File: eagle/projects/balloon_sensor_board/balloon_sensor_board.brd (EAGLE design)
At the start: 18 x 14 mm, 17 parts, among them J201 MOL-SL-4-RA, U201 PCT2075GVJ, U202 MS560702BA03-50

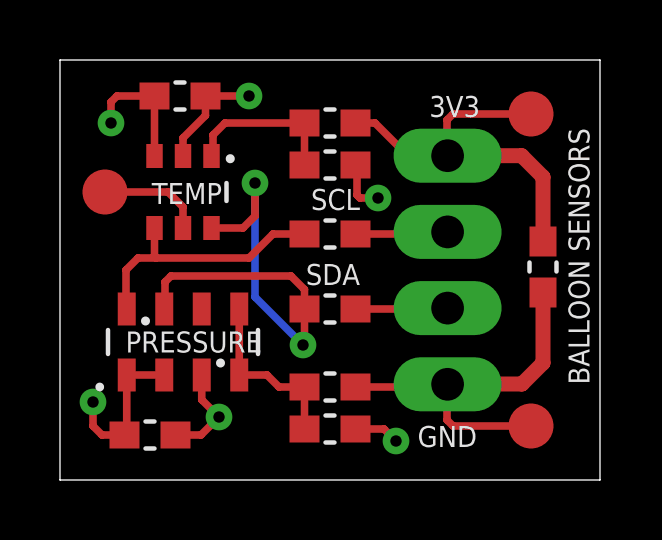
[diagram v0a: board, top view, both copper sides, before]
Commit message: adding all finalized gerber, schem, and bom files for Rev1 of HAT and balloon sensor boards
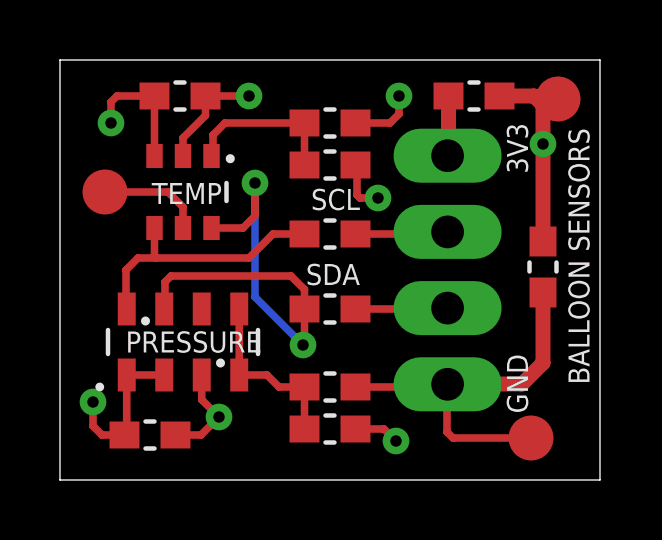
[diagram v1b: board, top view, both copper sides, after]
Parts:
- added R1: 0.0, daqcs:R0603
- moved TP201 1.03 mm to (16.6, 12.7)
- moved TP202 0.40 mm to (15.7, 1.40)
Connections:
- new net PP3V3_R: J201.1, R1.1
- net PP3V3: now also R1.2; no longer J201.1
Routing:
- net PP3V3: track 24.2 -> 20.0 mm, vias 3 -> 5
- net PP3V3_R: track 0.00 -> 2.00 mm

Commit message: added modified BOMs to remove non-component parts, samples, and column for a board instance multiplier
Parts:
- added BOM1: SL 70066 4PIN HOUSING, daqcs:BLANK
- added BOM2, BOM3, BOM4, BOM5: SL 70058 GOLD CRIMP, daqcs:BLANK
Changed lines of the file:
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@@
 </attributes>
 <variantdefs>
-<variantdef name="POR" current="yes"/>
+<variantdef name="POR"/>
 </variantdefs>
 <classes>
@@
 <attribute name="VALUE" x="17.119" y="11.692" size="0.254" layer="27" ratio="6"/>
 </element>
-<element name="R205" library="daqcs" package="R0603" value="0.0" x="9" y="11.9" populate="no" smashed="yes">
+<element name="R205" library="daqcs" package="R0603" value="0.0" x="9" y="11.9" smashed="yes">
 <attribute name="MANUFACTURER" value="Panasonic" x="9" y="11.9" size="1.778" layer="27" display="off"/>
 <attribute name="POWER" value="1/10W" x="9" y="11.9" size="1.778" layer="27" display="off"/>
@@
 <attribute name="VENDOR" value="Digi-key" x="9" y="11.9" size="1.778" layer="27" display="off"/>
 </element>
-<element name="R203" library="daqcs" package="R0603" value="0.0" x="9" y="1.7" populate="no" smashed="yes">
+<element name="R203" library="daqcs" package="R0603" value="0.0" x="9" y="1.7" smashed="yes">
 <attribute name="MANUFACTURER" value="Panasonic" x="9" y="1.7" size="1.778" layer="27" display="off"/>
 <attribute name="POWER" value="1/10W" x="9" y="1.7" size="1.778" layer="27" display="off"/>
@@
 <attribute name="MANUFACTURER_PN" value="ERJ-3GEY0R00V" x="13.8" y="12.8" size="1.778" layer="27" display="off"/>
 </element>
+<element name="BOM1" library="daqcs" package="BLANK" value="SL 70066 4PIN HOUSING" x="18.8" y="13.7">
+<attribute name="MANUFACTURER_PN" value="0050579404" x="18.8" y="13.7" size="1.778" layer="27" display="off"/>
+<attribute name="MANUFACTURER" value="Molex" x="18.8" y="13.7" size="1.778" layer="27" display="off"/>
+<attribute name="DATASHEET" value="HW/docs/projects/raspi_zero_power_sensor_hat/datasheets/connectors/uart_1wire_power_battery/050579402_sd.pdf" x="18.8" y="13.7" size="1.778" layer="27" display="off"/>
+<attribute name="VENDOR_PN" value="WM2902-ND" x="18.8" y="13.7" size="1.778" layer="27" display="off"/>
+<attribute name="VENDOR" value="Digi-key" x="18.8" y="13.7" size="1.778" layer="27" display="off"/>
+</element>
+<element name="BOM2" library="daqcs" package="BLANK" value="SL 70058 GOLD CRIMP" x="18.9" y="12.7">
+<attribute name="MANUFACTURER_PN" value="0016020087" x="18.9" y="12.7" size="1.778" layer="27" display="off"/>
+<attribute name="MANUFACTURER" value="Molex" x="18.9" y="12.7" size="1.778" layer="27" display="off"/>
+<attribute name="DATASHEET" value="HW/docs/projects/raspi_zero_power_sensor_hat/datasheets/connectors/uart_1wire_power_battery/016020087_sd.pdf" x="18.9" y="12.7" size="1.778" layer="27" display="off"/>
+<attribute name="VENDOR_PN" value="WM2512CT-ND" x="18.9" y="12.7" size="1.778" layer="27" display="off"/>
+<attribute name="VENDOR" value="Digi-key" x="18.9" y="12.7" size="1.778" layer="27" display="off"/>
+</element>
+<element name="BOM3" library="daqcs" package="BLANK" value="SL 70058 GOLD CRIMP" x="19" y="12">
+<attribute name="MANUFACTURER_PN" value="0016020087" x="19" y="12" size="1.778" layer="27" display="off"/>
+<attribute name="MANUFACTURER" value="Molex" x="19" y="12" size="1.778" layer="27" display="off"/>
+<attribute name="DATASHEET" value="HW/docs/projects/raspi_zero_power_sensor_hat/datasheets/connectors/uart_1wire_power_battery/016020087_sd.pdf" x="19" y="12" size="1.778" layer="27" display="off"/>
+<attribute name="VENDOR_PN" value="WM2512CT-ND" x="19" y="12" size="1.778" layer="27" display="off"/>
+<attribute name="VENDOR" value="Digi-key" x="19" y="12" size="1.778" layer="27" display="off"/>
+</element>
+<element name="BOM4" library="daqcs" package="BLANK" value="SL 70058 GOLD CRIMP" x="19.1" y="11.3">
+<attribute name="MANUFACTURER_PN" value="0016020087" x="19.1" y="11.3" size="1.778" layer="27" display="off"/>
+<attribute name="MANUFACTURER" value="Molex" x="19.1" y="11.3" size="1.778" layer="27" display="off"/>
+<attribute name="DATASHEET" value="HW/docs/projects/raspi_zero_power_sensor_hat/datasheets/connectors/uart_1wire_power_battery/016020087_sd.pdf" x="19.1" y="11.3" size="1.778" layer="27" display="off"/>
+<attribute name="VENDOR_PN" value="WM2512CT-ND" x="19.1" y="11.3" size="1.778" layer="27" display="off"/>
+<attribute name="VENDOR" value="Digi-key" x="19.1" y="11.3" size="1.778" layer="27" display="off"/>
+</element>
+<element name="BOM5" library="daqcs" package="BLANK" value="SL 70058 GOLD CRIMP" x="19.2" y="10.6">
+<attribute name="MANUFACTURER_PN" value="0016020087" x="19.2" y="10.6" size="1.778" layer="27" display="off"/>
+<attribute name="MANUFACTURER" value="Molex" x="19.2" y="10.6" size="1.778" layer="27" display="off"/>
+<attribute name="DATASHEET" value="HW/docs/projects/raspi_zero_power_sensor_hat/datasheets/connectors/uart_1wire_power_battery/016020087_sd.pdf" x="19.2" y="10.6" size="1.778" layer="27" display="off"/>
+<attribute name="VENDOR_PN" value="WM2512CT-ND" x="19.2" y="10.6" size="1.778" layer="27" display="off"/>
+<attribute name="VENDOR" value="Digi-key" x="19.2" y="10.6" size="1.778" layer="27" display="off"/>
+</element>
 </elements>
